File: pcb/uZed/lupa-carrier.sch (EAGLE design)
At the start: 93 parts, among them K1 694108105102

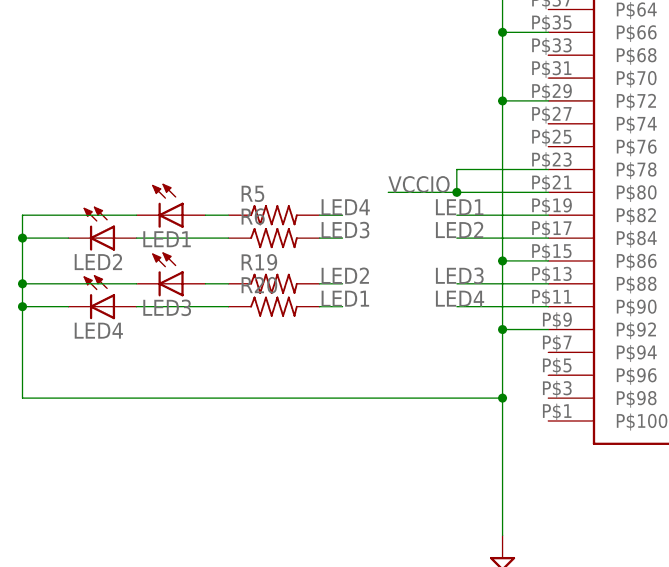
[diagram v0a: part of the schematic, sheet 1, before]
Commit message: added partslist for lupa carrier board
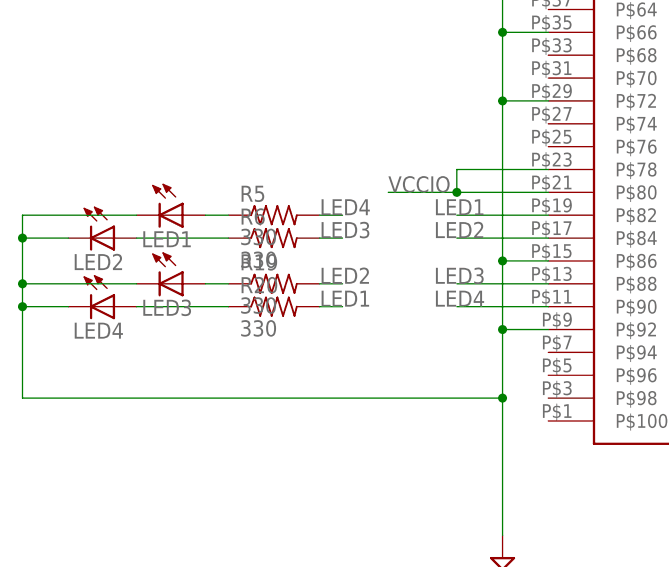
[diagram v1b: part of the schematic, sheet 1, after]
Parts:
- C22, C23, C26, C27: value (none) -> .1uF
- R19, R20, R5, R6: value (none) -> 330
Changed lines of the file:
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@@
 <part name="R27" library="rcl" library_urn="urn:adsk.eagle:library:334" deviceset="R-US_" device="R0603" package3d_urn="urn:adsk.eagle:package:23555/2" value="1.5M"/>
 <part name="R28" library="rcl" library_urn="urn:adsk.eagle:library:334" deviceset="R-US_" device="R0603" package3d_urn="urn:adsk.eagle:package:23555/2" value="500k"/>
-<part name="C22" library="rcl" library_urn="urn:adsk.eagle:library:334" deviceset="C-EU" device="C0603" package3d_urn="urn:adsk.eagle:package:23616/2"/>
-<part name="C23" library="rcl" library_urn="urn:adsk.eagle:library:334" deviceset="C-EU" device="C0603" package3d_urn="urn:adsk.eagle:package:23616/2"/>
+<part name="C22" library="rcl" library_urn="urn:adsk.eagle:library:334" deviceset="C-EU" device="C0603" package3d_urn="urn:adsk.eagle:package:23616/2" value=".1uF"/>
+<part name="C23" library="rcl" library_urn="urn:adsk.eagle:library:334" deviceset="C-EU" device="C0603" package3d_urn="urn:adsk.eagle:package:23616/2" value=".1uF"/>
 <part name="C24" library="rcl" library_urn="urn:adsk.eagle:library:334" deviceset="C-EU" device="C0603" package3d_urn="urn:adsk.eagle:package:23616/2" value=".1uf"/>
 <part name="C25" library="rcl" library_urn="urn:adsk.eagle:library:334" deviceset="C-EU" device="C0603" package3d_urn="urn:adsk.eagle:package:23616/2" value=".1uf"/>
-<part name="C26" library="rcl" library_urn="urn:adsk.eagle:library:334" deviceset="C-EU" device="C0603" package3d_urn="urn:adsk.eagle:package:23616/2"/>
-<part name="C27" library="rcl" library_urn="urn:adsk.eagle:library:334" deviceset="C-EU" device="C0603" package3d_urn="urn:adsk.eagle:package:23616/2"/>
+<part name="C26" library="rcl" library_urn="urn:adsk.eagle:library:334" deviceset="C-EU" device="C0603" package3d_urn="urn:adsk.eagle:package:23616/2" value=".1uF"/>
+<part name="C27" library="rcl" library_urn="urn:adsk.eagle:library:334" deviceset="C-EU" device="C0603" package3d_urn="urn:adsk.eagle:package:23616/2" value=".1uF"/>
 <part name="U$5" library="lupa300-components" deviceset="ADP7158ARDZ-2.5-R7CT-ND" device=""/>
 <part name="C6" library="rcl" library_urn="urn:adsk.eagle:library:334" deviceset="C-US" device="C0603" package3d_urn="urn:adsk.eagle:package:23616/2" value="10uF"/>
@@
 <part name="SPI_EN" library="testpad" library_urn="urn:adsk.eagle:library:385" deviceset="TP" device="TP08R" package3d_urn="urn:adsk.eagle:package:27956/1"/>
 <part name="POW_EN" library="testpad" library_urn="urn:adsk.eagle:library:385" deviceset="TP" device="TP08R" package3d_urn="urn:adsk.eagle:package:27956/1"/>
-<part name="R5" library="resistor" library_urn="urn:adsk.eagle:library:348" deviceset="R-US_" device="R0603" package3d_urn="urn:adsk.eagle:package:26057/1"/>
-<part name="R6" library="resistor" library_urn="urn:adsk.eagle:library:348" deviceset="R-US_" device="R0603" package3d_urn="urn:adsk.eagle:package:26057/1"/>
-<part name="R19" library="resistor" library_urn="urn:adsk.eagle:library:348" deviceset="R-US_" device="R0603" package3d_urn="urn:adsk.eagle:package:26057/1"/>
-<part name="R20" library="resistor" library_urn="urn:adsk.eagle:library:348" deviceset="R-US_" device="R0603" package3d_urn="urn:adsk.eagle:package:26057/1"/>
+<part name="R5" library="resistor" library_urn="urn:adsk.eagle:library:348" deviceset="R-US_" device="R0603" package3d_urn="urn:adsk.eagle:package:26057/1" value="330"/>
+<part name="R6" library="resistor" library_urn="urn:adsk.eagle:library:348" deviceset="R-US_" device="R0603" package3d_urn="urn:adsk.eagle:package:26057/1" value="330"/>
+<part name="R19" library="resistor" library_urn="urn:adsk.eagle:library:348" deviceset="R-US_" device="R0603" package3d_urn="urn:adsk.eagle:package:26057/1" value="330"/>
+<part name="R20" library="resistor" library_urn="urn:adsk.eagle:library:348" deviceset="R-US_" device="R0603" package3d_urn="urn:adsk.eagle:package:26057/1" value="330"/>
 <part name="LED1" library="led" library_urn="urn:adsk.eagle:library:259" deviceset="LED" device="CHIPLED_0805" package3d_urn="urn:adsk.eagle:package:15821/2"/>
 <part name="LED2" library="led" library_urn="urn:adsk.eagle:library:259" deviceset="LED" device="CHIPLED_0805" package3d_urn="urn:adsk.eagle:package:15821/2"/>

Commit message: updated with schematic
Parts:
- removed C10, C8, C9: .1uF, rcl:C-USC0603
- removed R13, R14: 1k, rcl:R-US_R0603
- removed R15: 3k74, rcl:R-US_R0603
- removed R16: 0, rcl:R-US_R0603
- removed R17: 3k, rcl:R-US_R0603
- removed R18: 100k, rcl:R-US_R0603
- removed U$10: AP331A, lupa300-components:AP331A
- removed U$9: TL431A, lupa300-components:TL431A
- added C21, C28: .1uF, rcl:C-EUC0603K
- added C32: (no value), rcl:C-USC0603
- added J5, J6: HDMI-TYPE-A-RECEPTICALFCI10029449, saanlima:HDMI-TYPE-A-RECEPTICALFCI10029449
- added OFF, ON: (no value), adafruit:LEDCHIPLED_0805
- added PCA9306: PCA9306, saanlima:PCA9306
- added R21, R8: 100K, rcl:R-US_R0603
- added R22, R32: 0, rcl:R-US_R0603
- added R29, R30, R31: 10K, rcl:R-US_R0603
- added RN3, RN4, RN5, RN6: 51, resistor-dil:2R-NEXB34V
- added RN7: 2k, resistor-dil:4R-N0603-ARV
- added U$17: BSS138, lupa300-components:BSS138
- added U$18: SI514, lupa300-components:SI514
- C22, C23, C26, C27: value .1uF -> (none)
- R12: value 1k5 -> 1k
- R19, R20, R5, R6: value 330 -> (none)
- renumbered U$12 to F1, U$13 to F2, U$16 to F3
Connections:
- removed net 2V5_REF: C8.1, R11.2, R12.1, U$9.K, U$9.REF
- removed net N$7: C10.1, R14.2, R15.1, U$10.N
- removed net N$9: C10.2, R16.1, R17.1, U$10.VOUT
- removed net VADJ_EN: R16.2, R18.2, U$11.EN
- new net 3V3: C32.1, PCA9306.VREF1, R22.2, R31.1, RN7A.1, RN7B.1, U$18.VDD
- new net DET_CONTROL: R31.2, U$17.G
- new net HDMI_OSC: JX2.P$54, U$18.CLK
- new net HDMI_PU: R22.1, RN3A.2, RN3B.2, RN4A.2, RN4B.2, RN5A.2, RN5B.2, RN6A.2, RN6B.2
- new net N$17: J5.DETECT, R29.2
- new net N$18: J6.DETECT, R30.1, U$17.D
- new net N$19: J6.SDA, PCA9306.SDA2, RN7D.2
- new net N$20: J6.SCL, PCA9306.SCL2, RN7C.2
- new net N$21: J5.+5V, R32.2
- new net N$24: OFF.A, R12.1
- new net N$34: C21.1, J6.SH1, J6.SH2, J6.SH3, J6.SH4, R8.2
- new net N$6: C28.1, J5.SH1, J5.SH2, J5.SH3, J5.SH4, R21.2
- new net P1_CLOCK+: J6.CLOCK+, JX1.P$35, RN3B.1
- new net P1_CLOCK-: J6.CLOCK-, JX1.P$37, RN3A.1
- new net P1_DATA0+: J6.DATA0+, JX1.P$29, RN4B.1
- new net P1_DATA0-: J6.DATA0-, JX1.P$31, RN4A.1
- new net P1_DATA1+: J6.DATA1+, JX1.P$23, RN5B.1
- new net P1_DATA1-: J6.DATA1-, JX1.P$25, RN5A.1
- new net P1_DATA2+: J6.DATA2+, JX1.P$17, RN6B.1
- new net P1_DATA2-: J6.DATA2-, JX1.P$19, RN6A.1
- new net P2_CLOCK+: J5.CLOCK+, JX1.P$67
- new net P2_CLOCK-: J5.CLOCK-, JX1.P$69
- new net P2_DATA0+: J5.DATA0+, JX1.P$61
- new net P2_DATA0-: J5.DATA0-, JX1.P$63
- new net P2_DATA1+: J5.DATA1+, JX1.P$53
- new net P2_DATA1-: J5.DATA1-, JX1.P$55
- new net P2_DATA2+: J5.DATA2+, JX1.P$47
- new net P2_DATA2-: J5.DATA2-, JX1.P$49
- new net SCL2: PCA9306.SCL1, RN7A.2
- new net SCLC: U$18.SCL
- new net SDA2: PCA9306.SDA1, RN7B.2
- new net SDAC: U$18.SDA
- net 5V: now also J6.+5V, PCA9306.EN, PCA9306.VREF2, R11.1, R30.2, R32.1, RN7C.1, RN7D.1; no longer R17.2
- net 5V_OFF: now also R12.2
- net GND: now also C21.2, C28.2, C32.2, J5.CLOCKSHIELD, J5.DATA0SHIELD, J5.DATA1SHIELD, J5.DATA2SHIELD, J5.DDC/CEC-GRND, J5.RES, J6.CLOCKSHIELD, J6.DATA0SHIELD, J6.DATA1SHIELD, J6.DATA2SHIELD, J6.DDC/CEC-GRND, J6.RES, OFF.C, ON.C, PCA9306.GND, R21.1, R29.1, R8.1, U$17.S, U$18.GND; no longer C8.2, C9.2, R13.1, R15.2, R18.1, U$10.VSS, U$9.A
- net N$5: now also ON.A, R11.2; no longer R12.2, R13.2, U$10.P
- net VCCIO_EN: now also U$11.EN; no longer R14.1
- net VIN: no longer C9.1, R11.1, U$10.VDD

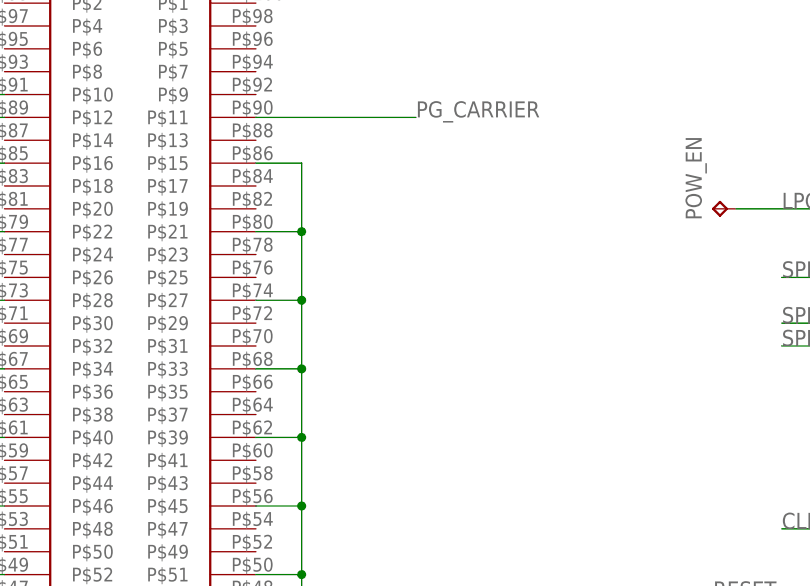
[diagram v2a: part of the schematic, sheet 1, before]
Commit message: beginning 4 layer hdmi board, discarded 6 layer approach
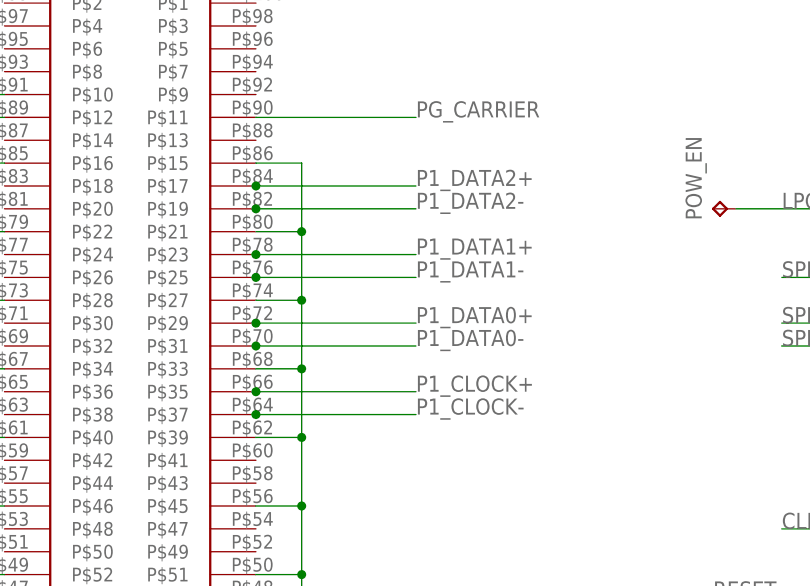
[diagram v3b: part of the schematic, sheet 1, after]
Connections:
- net P1_CLOCK+: now also JX2.P$35
- net P1_CLOCK-: now also JX2.P$37
- net P1_DATA0+: now also JX2.P$29
- net P1_DATA0-: now also JX2.P$31
- net P1_DATA1+: now also JX2.P$23
- net P1_DATA1-: now also JX2.P$25
- net P1_DATA2+: now also JX2.P$17
- net P1_DATA2-: now also JX2.P$19
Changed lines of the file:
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@@
 <label x="187.96" y="129.54" size="1.778" layer="95"/>
+</segment>
+<segment>
+<wire x1="63.5" y1="129.54" x2="81.28" y2="129.54" width="0.1524" layer="91"/>
+<label x="81.28" y="129.54" size="1.778" layer="95"/>
+<pinref part="JX2" gate="G$1" pin="P$17"/>
+<junction x="63.5" y="129.54"/>
 </segment>
 </net>
@@
 <label x="187.96" y="127" size="1.778" layer="95"/>
 </segment>
+<segment>
+<wire x1="63.5" y1="127" x2="81.28" y2="127" width="0.1524" layer="91"/>
+<label x="81.28" y="127" size="1.778" layer="95"/>
+<pinref part="JX2" gate="G$1" pin="P$19"/>
+<junction x="63.5" y="127"/>
+</segment>
 </net>
 <net name="P1_DATA1+" class="0">
@@
 <wire x1="170.18" y1="121.92" x2="187.96" y2="121.92" width="0.1524" layer="91"/>
 <label x="187.96" y="121.92" size="1.778" layer="95"/>
+</segment>
+<segment>
+<wire x1="63.5" y1="121.92" x2="81.28" y2="121.92" width="0.1524" layer="91"/>
+<label x="81.28" y="121.92" size="1.778" layer="95"/>
+<pinref part="JX2" gate="G$1" pin="P$23"/>
+<junction x="63.5" y="121.92"/>
 </segment>
 </net>
@@
 <label x="187.96" y="119.38" size="1.778" layer="95"/>
 </segment>
+<segment>
+<wire x1="63.5" y1="119.38" x2="81.28" y2="119.38" width="0.1524" layer="91"/>
+<label x="81.28" y="119.38" size="1.778" layer="95"/>
+<pinref part="JX2" gate="G$1" pin="P$25"/>
+<junction x="63.5" y="119.38"/>
+</segment>
 </net>
 <net name="P1_DATA0+" class="0">
@@
 <wire x1="170.18" y1="114.3" x2="187.96" y2="114.3" width="0.1524" layer="91"/>
 <label x="187.96" y="114.3" size="1.778" layer="95"/>
+</segment>
+<segment>
+<wire x1="63.5" y1="114.3" x2="81.28" y2="114.3" width="0.1524" layer="91"/>
+<label x="81.28" y="114.3" size="1.778" layer="95"/>
+<pinref part="JX2" gate="G$1" pin="P$29"/>
+<junction x="63.5" y="114.3"/>
 </segment>
 </net>
@@
 <label x="187.96" y="111.76" size="1.778" layer="95"/>
 </segment>
+<segment>
+<wire x1="63.5" y1="111.76" x2="81.28" y2="111.76" width="0.1524" layer="91"/>
+<label x="81.28" y="111.76" size="1.778" layer="95"/>
+<pinref part="JX2" gate="G$1" pin="P$31"/>
+<junction x="63.5" y="111.76"/>
+</segment>
 </net>
 <net name="P1_CLOCK+" class="0">
@@
 <wire x1="170.18" y1="106.68" x2="187.96" y2="106.68" width="0.1524" layer="91"/>
 <label x="187.96" y="106.68" size="1.778" layer="95"/>
+</segment>
+<segment>
+<wire x1="63.5" y1="106.68" x2="81.28" y2="106.68" width="0.1524" layer="91"/>
+<label x="81.28" y="106.68" size="1.778" layer="95"/>
+<pinref part="JX2" gate="G$1" pin="P$35"/>
+<junction x="63.5" y="106.68"/>
 </segment>
 </net>
@@
 <label x="187.96" y="104.14" size="1.778" layer="95"/>
 </segment>
+<segment>
+<wire x1="63.5" y1="104.14" x2="81.28" y2="104.14" width="0.1524" layer="91"/>
+<label x="81.28" y="104.14" size="1.778" layer="95"/>
+<pinref part="JX2" gate="G$1" pin="P$37"/>
+<junction x="63.5" y="104.14"/>
+</segment>
 </net>

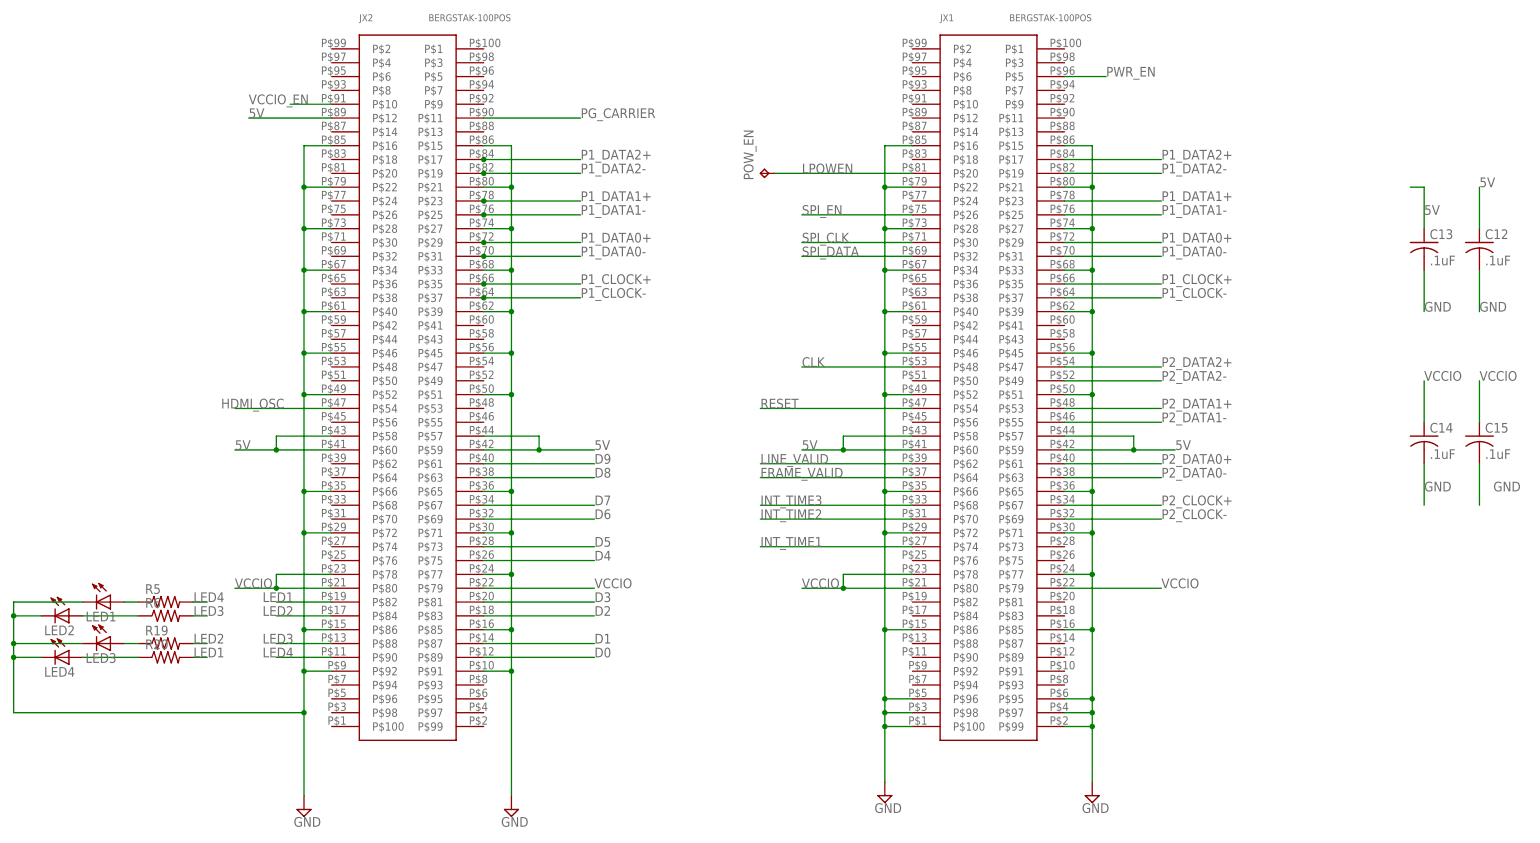
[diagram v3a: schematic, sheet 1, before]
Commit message: routed hdmi and lupa data lines
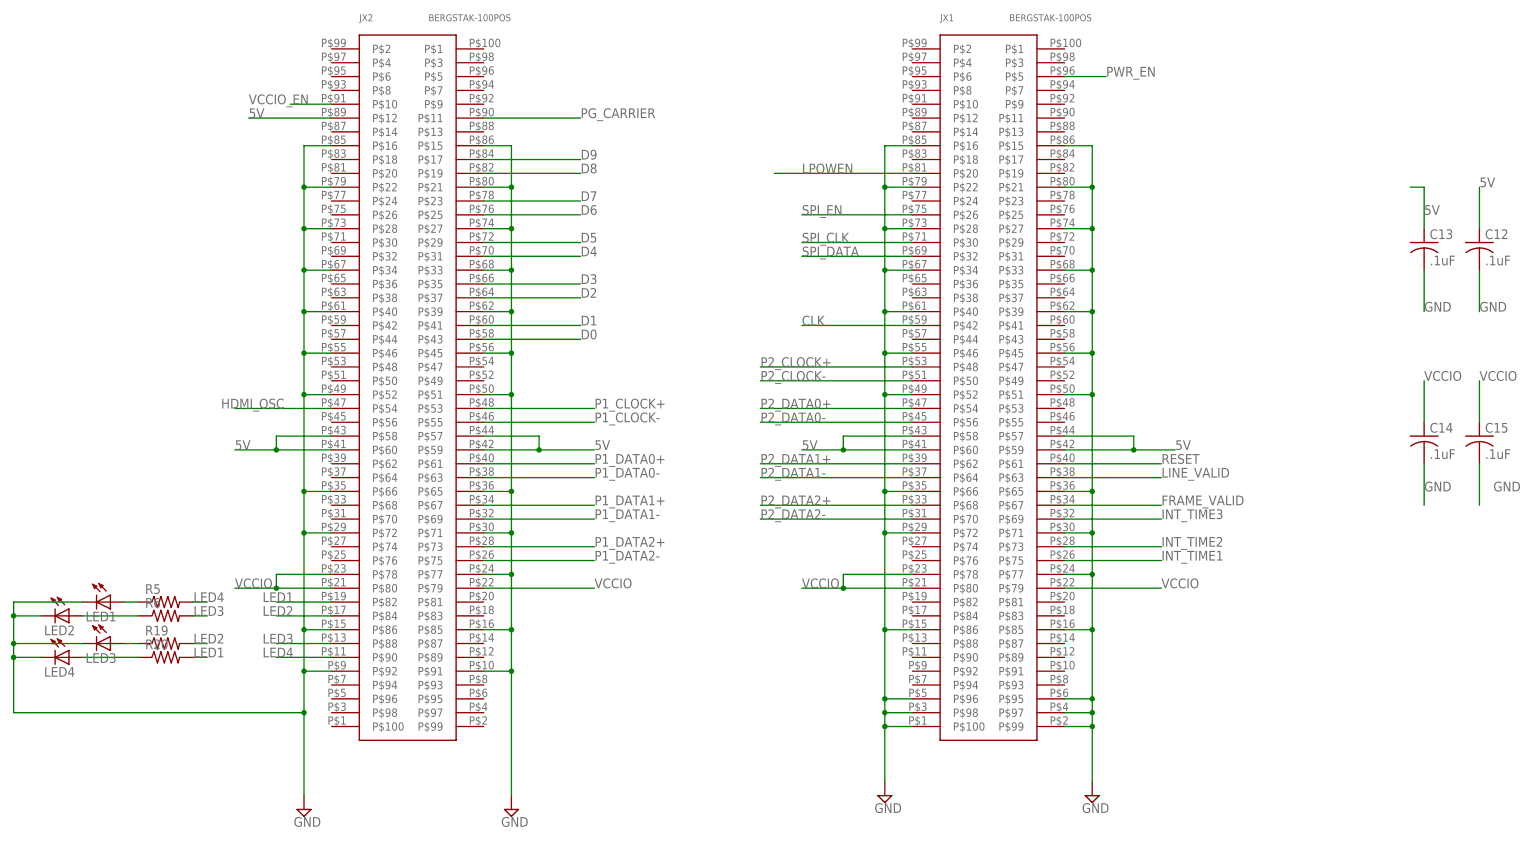
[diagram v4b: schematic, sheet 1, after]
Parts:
- removed FR_VAL, INT1, INT2, INT3, LN_VAL, POW_EN, RESET, SPI_CLK, SPI_DATA, SPI_EN: TPTP08R, testpad:TPTP08R
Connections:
- net CLK: now also JX1.P$42; no longer JX1.P$48
- net D0: now also JX2.P$43; no longer JX2.P$89
- net D1: now also JX2.P$41; no longer JX2.P$87
- net D2: now also JX2.P$37; no longer JX2.P$83
- net D3: now also JX2.P$35; no longer JX2.P$81
- net D4: now also JX2.P$31; no longer JX2.P$75
- net D5: now also JX2.P$29; no longer JX2.P$73
- net D6: now also JX2.P$25; no longer JX2.P$69
- net D7: now also JX2.P$23; no longer JX2.P$67
- net D8: now also JX2.P$19; no longer JX2.P$63
- net D9: now also JX2.P$17; no longer JX2.P$61
- net FRAME_VALID: now also JX1.P$67; no longer FR_VAL.TP, JX1.P$64
- net INT_TIME1: now also JX1.P$75; no longer INT1.TP, JX1.P$74
- net INT_TIME2: now also JX1.P$73; no longer INT2.TP, JX1.P$70
- net INT_TIME3: now also JX1.P$69; no longer INT3.TP, JX1.P$68
- net LINE_VALID: now also JX1.P$63; no longer JX1.P$62, LN_VAL.TP
- net LPOWEN: no longer POW_EN.TP
- net P1_CLOCK+: now also JX2.P$53; no longer JX1.P$35, JX2.P$35
- net P1_CLOCK-: now also JX2.P$55; no longer JX1.P$37, JX2.P$37
- net P1_DATA0+: now also JX2.P$61; no longer JX1.P$29, JX2.P$29
- net P1_DATA0-: now also JX2.P$63; no longer JX1.P$31, JX2.P$31
- net P1_DATA1+: now also JX2.P$67; no longer JX1.P$23, JX2.P$23
- net P1_DATA1-: now also JX2.P$69; no longer JX1.P$25, JX2.P$25
- net P1_DATA2+: now also JX2.P$73; no longer JX1.P$17, JX2.P$17
- net P1_DATA2-: now also JX2.P$75; no longer JX1.P$19, JX2.P$19
- net P2_CLOCK+: now also JX1.P$48; no longer JX1.P$67
- net P2_CLOCK-: now also JX1.P$50; no longer JX1.P$69
- net P2_DATA0+: now also JX1.P$54; no longer JX1.P$61
- net P2_DATA0-: now also JX1.P$56; no longer JX1.P$63
- net P2_DATA1+: now also JX1.P$62; no longer JX1.P$53
- net P2_DATA1-: now also JX1.P$64; no longer JX1.P$55
- net P2_DATA2+: now also JX1.P$68; no longer JX1.P$47
- net P2_DATA2-: now also JX1.P$70; no longer JX1.P$49
- net RESET: now also JX1.P$61; no longer JX1.P$54, RESET.TP
- net SPI_CLK: no longer SPI_CLK.TP
- net SPI_DATA: no longer SPI_DATA.TP
- net SPI_EN: no longer SPI_EN.TP

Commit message: more layout
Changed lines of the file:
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@@
-</segment>
-</net>
-<net name="VDDA" class="0">
-<segment>
-<pinref part="F2" gate="G$1" pin="1"/>
-<wire x1="55.88" y1="33.02" x2="50.8" y2="33.02" width="0.1524" layer="91"/>
-<pinref part="C5" gate="G$1" pin="1"/>
-<wire x1="50.8" y1="33.02" x2="50.8" y2="30.48" width="0.1524" layer="91"/>
-<wire x1="50.8" y1="33.02" x2="40.64" y2="33.02" width="0.1524" layer="91"/>
-<label x="40.64" y="33.02" size="1.778" layer="95"/>
-<junction x="50.8" y="33.02"/>
 </segment>
 </net>
@@
 </segment>
 </net>
+<net name="VDDA" class="0">
+<segment>
+<pinref part="F2" gate="G$1" pin="1"/>
+<wire x1="55.88" y1="33.02" x2="50.8" y2="33.02" width="0.1524" layer="91"/>
+<pinref part="C5" gate="G$1" pin="1"/>
+<wire x1="50.8" y1="33.02" x2="40.64" y2="33.02" width="0.1524" layer="91"/>
+<wire x1="50.8" y1="30.48" x2="50.8" y2="33.02" width="0.1524" layer="91"/>
+<junction x="50.8" y="33.02"/>
+<label x="40.64" y="33.02" size="1.778" layer="95"/>
+</segment>
+</net>
